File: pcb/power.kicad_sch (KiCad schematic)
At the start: 30 parts, among them U3 TLV75533PDBVR, U4 BQ24078RGTR

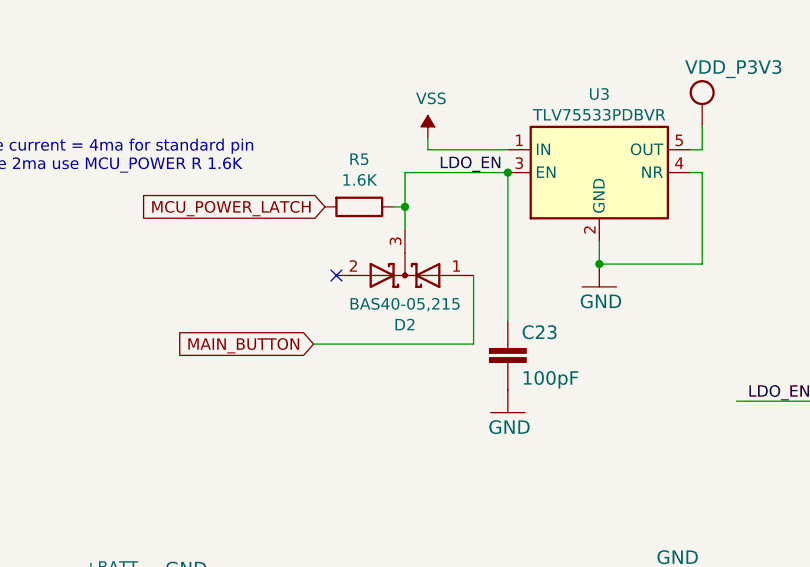
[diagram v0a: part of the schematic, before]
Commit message: [pcb] fixed symbol table issue
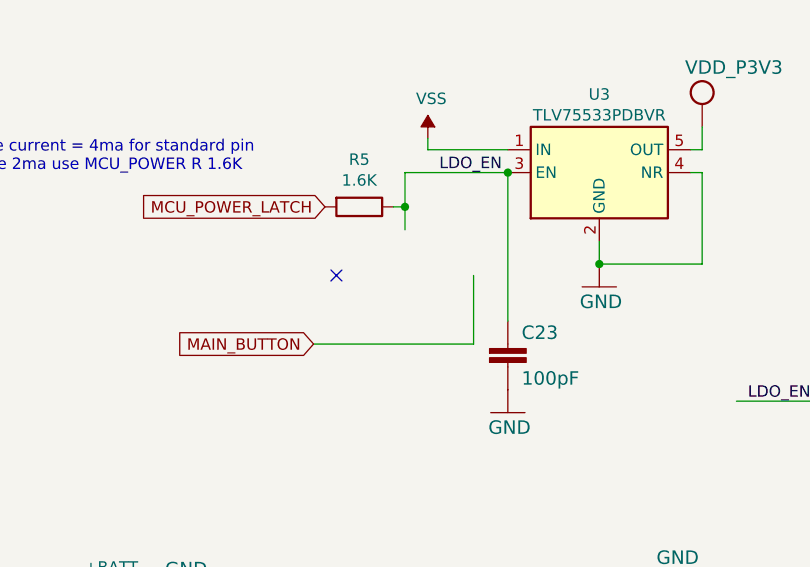
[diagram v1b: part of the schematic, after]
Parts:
- removed D2: BAS40-05,215, Package_TO_SOT_SMD:SOT-23, symbol nRF52832_qfaa-rescue:D_Schottky_x2_KCom_AAK-Device
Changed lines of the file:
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@@
     (pin "1")
-  )
-  (symbol (lib_id "nRF52832_qfaa-rescue:D_Schottky_x2_KCom_AAK-Device") (at 160.02 35.56 180) (unit 1)
-    (in_bom yes) (on_board yes)
-    (property "Reference" "D2" (id 0) (at 160.02 41.0718 0))
-    (property "Value" "BAS40-05,215" (id 1) (at 160.02 38.7604 0))
-    (property "Footprint" "Package_TO_SOT_SMD:SOT-23" (id 2) (at 160.02 35.56 0)
-      (effects (font (size 1.27 1.27)) hide)
-    )
-    (property "Datasheet" "~" (id 3) (at 160.02 35.56 0)
-      (effects (font (size 1.27 1.27)) hide)
-    )
-    (property "LCSC" "C85391" (id 4) (at 160.02 35.56 0)
-      (effects (font (size 1.27 1.27)) hide)
-    )
-    (pin "1")
-    (pin "2")
-    (pin "3")
   )
   (symbol (lib_id "nRF52832_qfaa-eagle-import:VCC") (at 212.09 16.51 0) (unit 1)

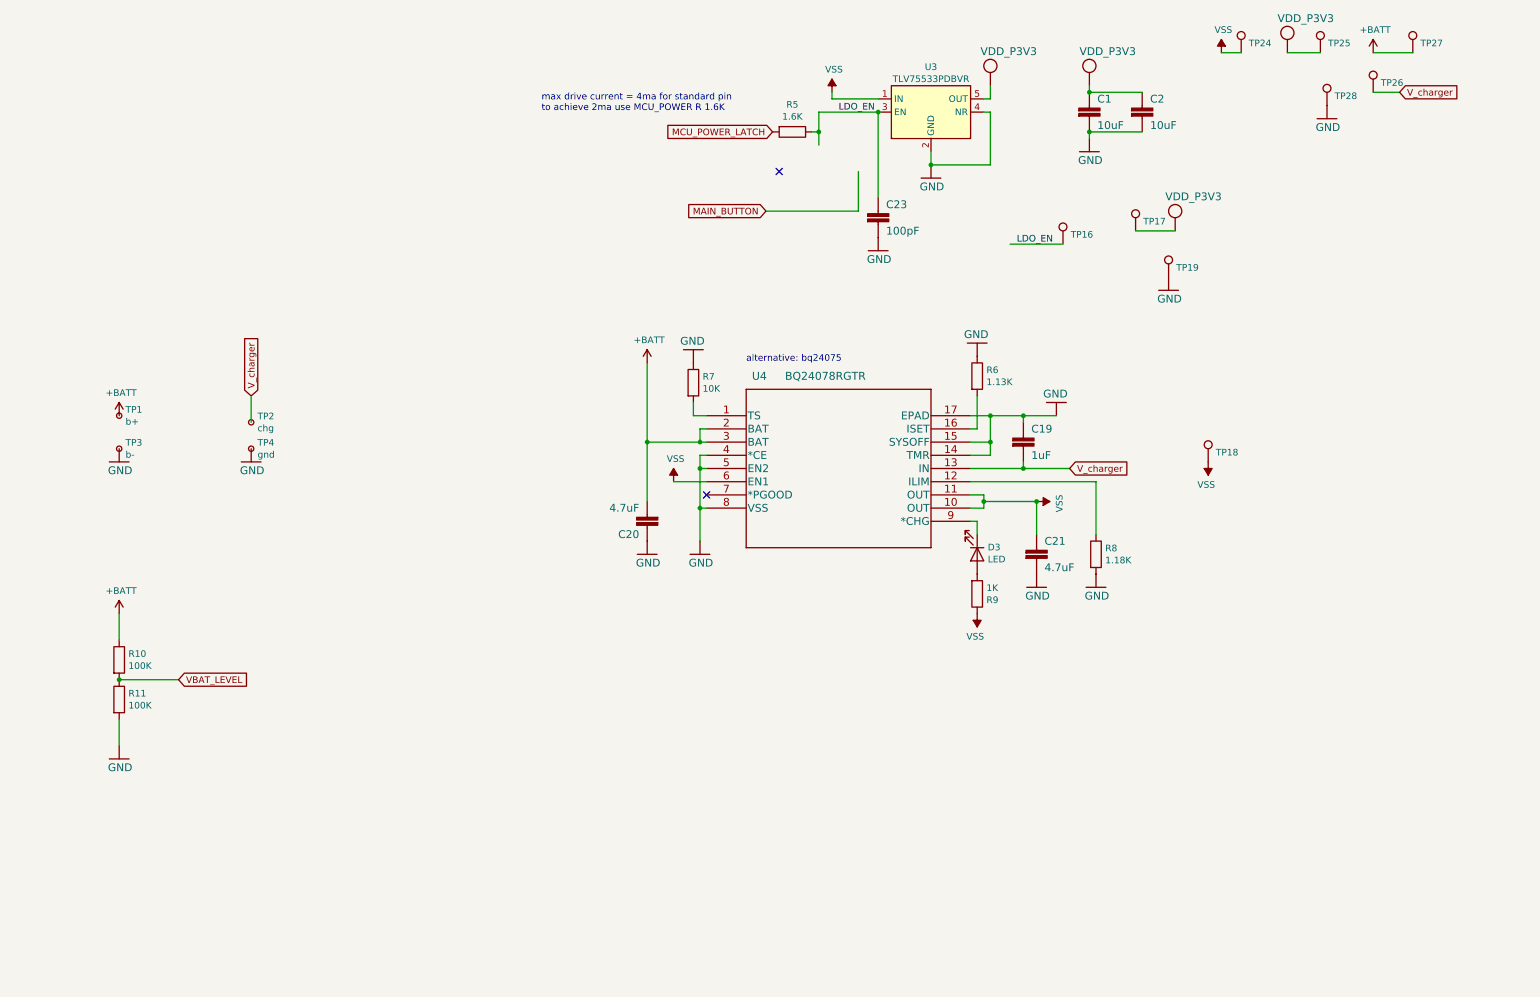
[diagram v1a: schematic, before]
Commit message: [pcb] finalizing layout of v1.3, only testpoints, teardrops and DRC is left
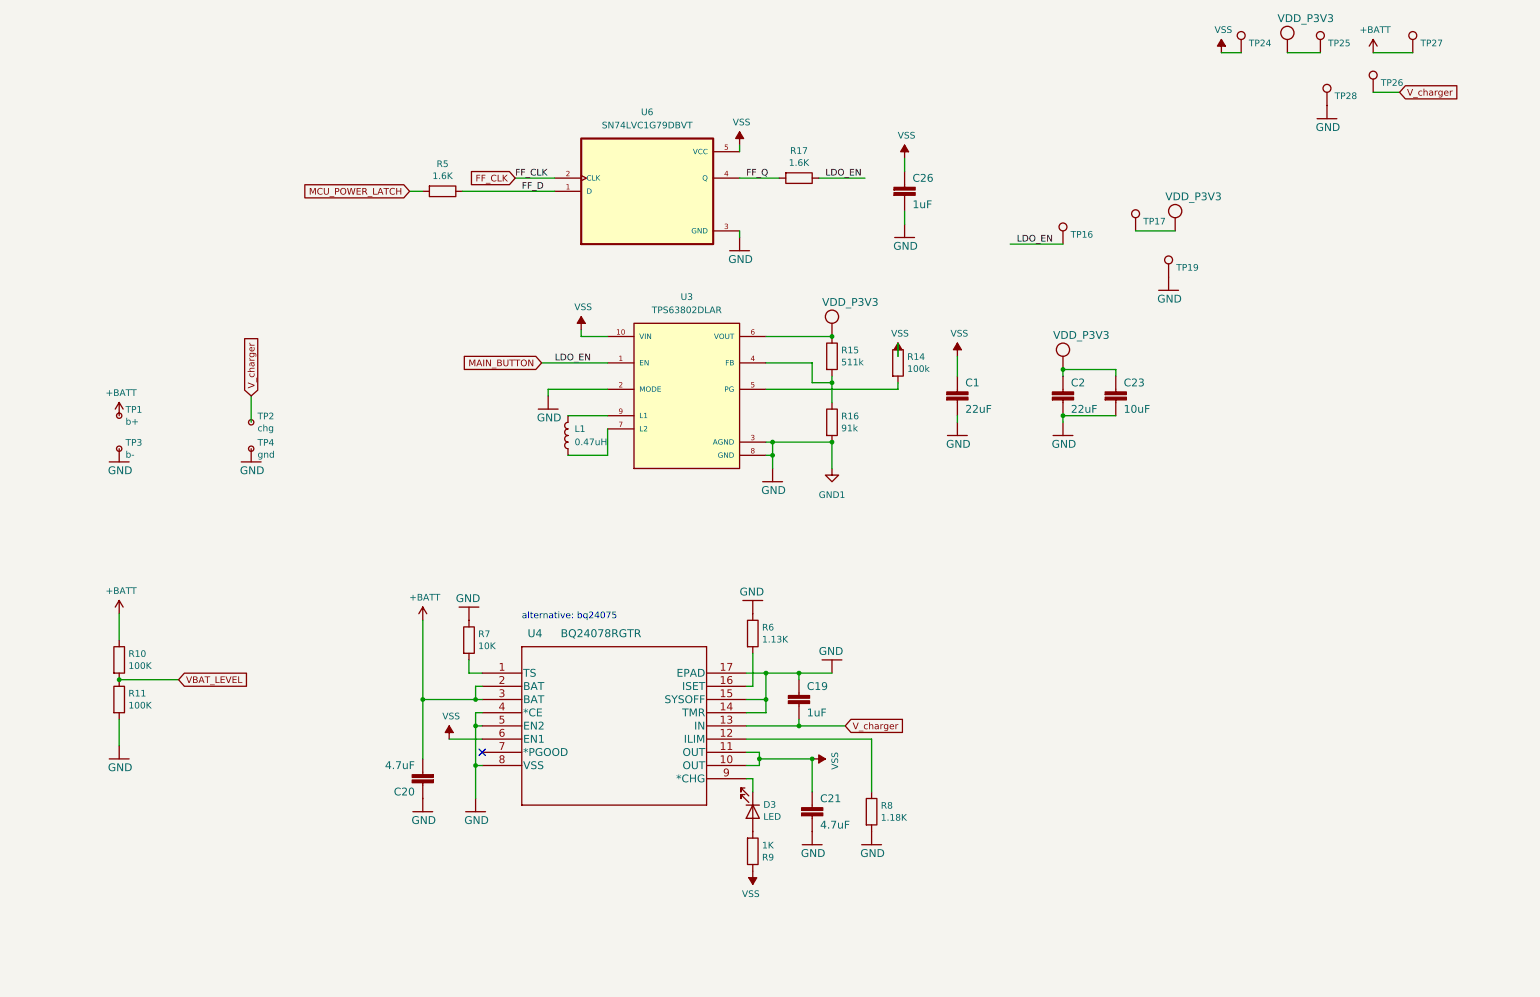
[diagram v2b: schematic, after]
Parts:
- removed TP18: TestPoint, TestPoint:TestPoint_Pad_D1.0mm, symbol Connector:TestPoint
- removed U3: TLV75533PDBVR, Package_TO_SOT_SMD:SOT-23-5, symbol Regulator_Linear:TPS73133DBV
- added C26: 1uF, Capacitor_SMD:C_0402_1005Metric, symbol nRF52832_qfaa-eagle-import:CAPACITOR_0402_N
- added L1: 0.47uH, Inductor_SMD:L_1008_2520Metric, symbol Device:L
- added R14: 100k, Resistor_SMD:R_0402_1005Metric, symbol Device:R
- added R15: 511k, Resistor_SMD:R_0402_1005Metric, symbol Device:R
- added R16: 91k, Resistor_SMD:R_0402_1005Metric, symbol Device:R
- added R17: 1.6K, Resistor_SMD:R_0402_1005Metric, symbol Device:R
- added U3: TPS63802DLAR, VREG_TPS63802DLAR, symbol custom:TPS63802DLAR
- added U6: SN74LVC1G79DBVT, Package_TO_SOT_SMD:SOT-23-5, symbol custom:SN74LVC1G79DBVT
- C1, C2: value 10uF -> 22uF; footprint Capacitor_SMD:C_0402_1005Metric -> Capacitor_SMD:C_0603_1608Metric; LCSC C15525 -> (none)
- C23: value 100pF -> 10uF; LCSC C1546 -> C15525
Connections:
- net GND: now also C26.2, R16.2, U3.2 (MODE), U3.3 (AGND), U3.8 (GND), U6.3 (GND)
- net MAIN_BUTTON: now also TP16.1, R17.1, U3.1 (EN)
- net VCC: now also C23.1, R15.1, U3.6 (VOUT); no longer C1.1
- net VSS: now also C1.1, C26.1, R14.1, U3.10 (VIN), U6.5 (VCC)
- removed net LDO_EN: C23.1, R5.1, TP16.1
- new net: R15.2, R16.1, U3.4 (FB)
- new net: R14.2, U3.5 (PG)
- new net: L1.1, U3.7 (L2)
- new net: L1.2, U3.9 (L1)
- new net FF_CLK: U6.2 (CLK)
- new net FF_D: R5.1, U6.1 (D)
- new net FF_Q: R17.2, U6.4 (Q)
- no-connect marks 2 -> 1
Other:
- note removed: "max drive current = 4ma for standard pin to achieve 2ma use MCU_POWER R 1.6K"
- moved on the sheet: C19, C20, C21, D3, R6, R7, R8, R9, U4

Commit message: [pcb] finalized layout of v1.3
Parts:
- removed TP17: TestPoint, TestPoint:TestPoint_Pad_D1.0mm, symbol Connector:TestPoint
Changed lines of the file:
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@@
-    (stroke (width 0) (type default) (color 0 0 0 0))
-  )
-  (wire (pts (xy 220.98 46.99) (xy 228.6 46.99))
     (stroke (width 0) (type default) (color 0 0 0 0))
   )
@@
     (pin "2")
   )
-  (symbol (lib_id "nRF52832_qfaa-eagle-import:VCC") (at 228.6 44.45 0) (unit 1)
-    (in_bom yes) (on_board yes)
-    (property "Reference" "#VDD_NRF01" (id 0) (at 228.6 44.45 0)
-      (effects (font (size 1.27 1.27)) hide)
-    )
-    (property "Value" "VDD_P3V3" (id 1) (at 226.695 41.275 0)
-      (effects (font (size 1.4986 1.4986)) (justify left bottom))
-    )
-    (property "Footprint" "" (id 2) (at 228.6 44.45 0)
-      (effects (font (size 1.27 1.27)) hide)
-    )
-    (property "Datasheet" "" (id 3) (at 228.6 44.45 0)
-      (effects (font (size 1.27 1.27)) hide)
-    )
-    (pin "1")
-  )
   (symbol (lib_id "Connector:TestPoint") (at 274.32 12.7 0) (unit 1)
     (in_bom yes) (on_board yes)
@@
     (pin "5")
   )
-  (symbol (lib_id "Connector:TestPoint") (at 220.98 46.99 0) (unit 1)
-    (in_bom yes) (on_board yes)
-    (property "Reference" "TP17" (id 0) (at 222.4532 45.1612 0)
-      (effects (font (size 1.27 1.27)) (justify left))
-    )
-    (property "Value" "TestPoint" (id 1) (at 222.4532 46.3042 0)
-      (effects (font (size 1.27 1.27)) (justify left) hide)
-    )
-    (property "Footprint" "TestPoint:TestPoint_Pad_D1.0mm" (id 2) (at 226.06 46.99 0)
-      (effects (font (size 1.27 1.27)) hide)
-    )
-    (property "Datasheet" "~" (id 3) (at 226.06 46.99 0)
-      (effects (font (size 1.27 1.27)) hide)
-    )
-    (pin "1")
-  )
   (symbol (lib_id "nRF52832_qfaa-eagle-import:VCC") (at 207.01 71.12 0) (unit 1)

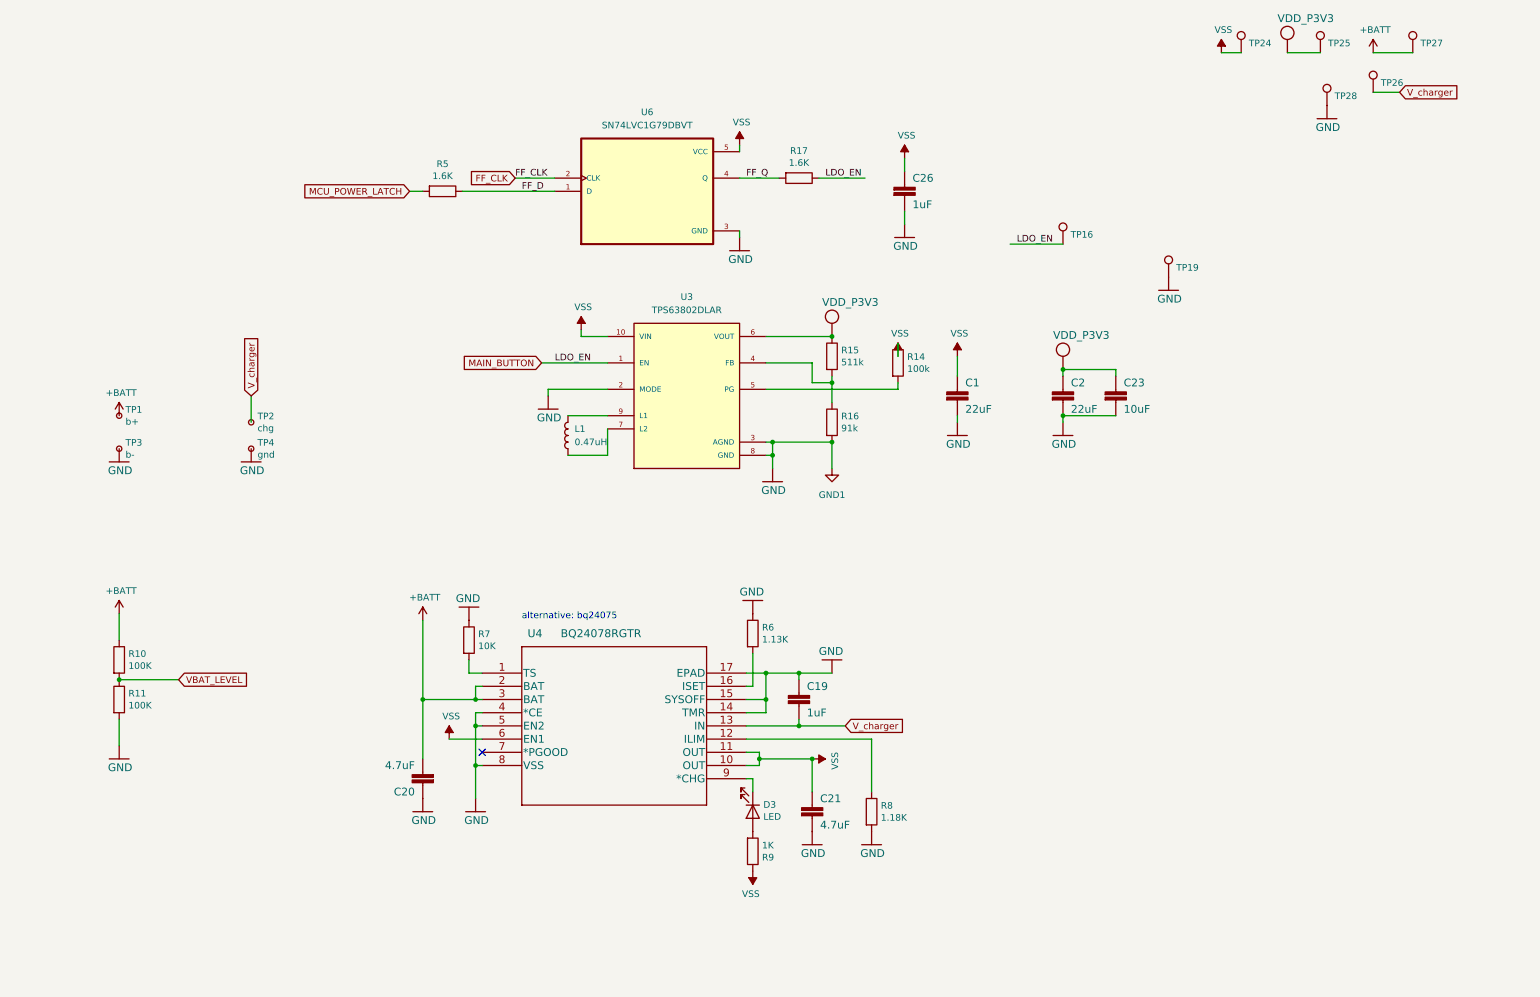
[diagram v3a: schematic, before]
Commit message: [pcb] finalized 1.3: added testpoints, fixed DRC errors
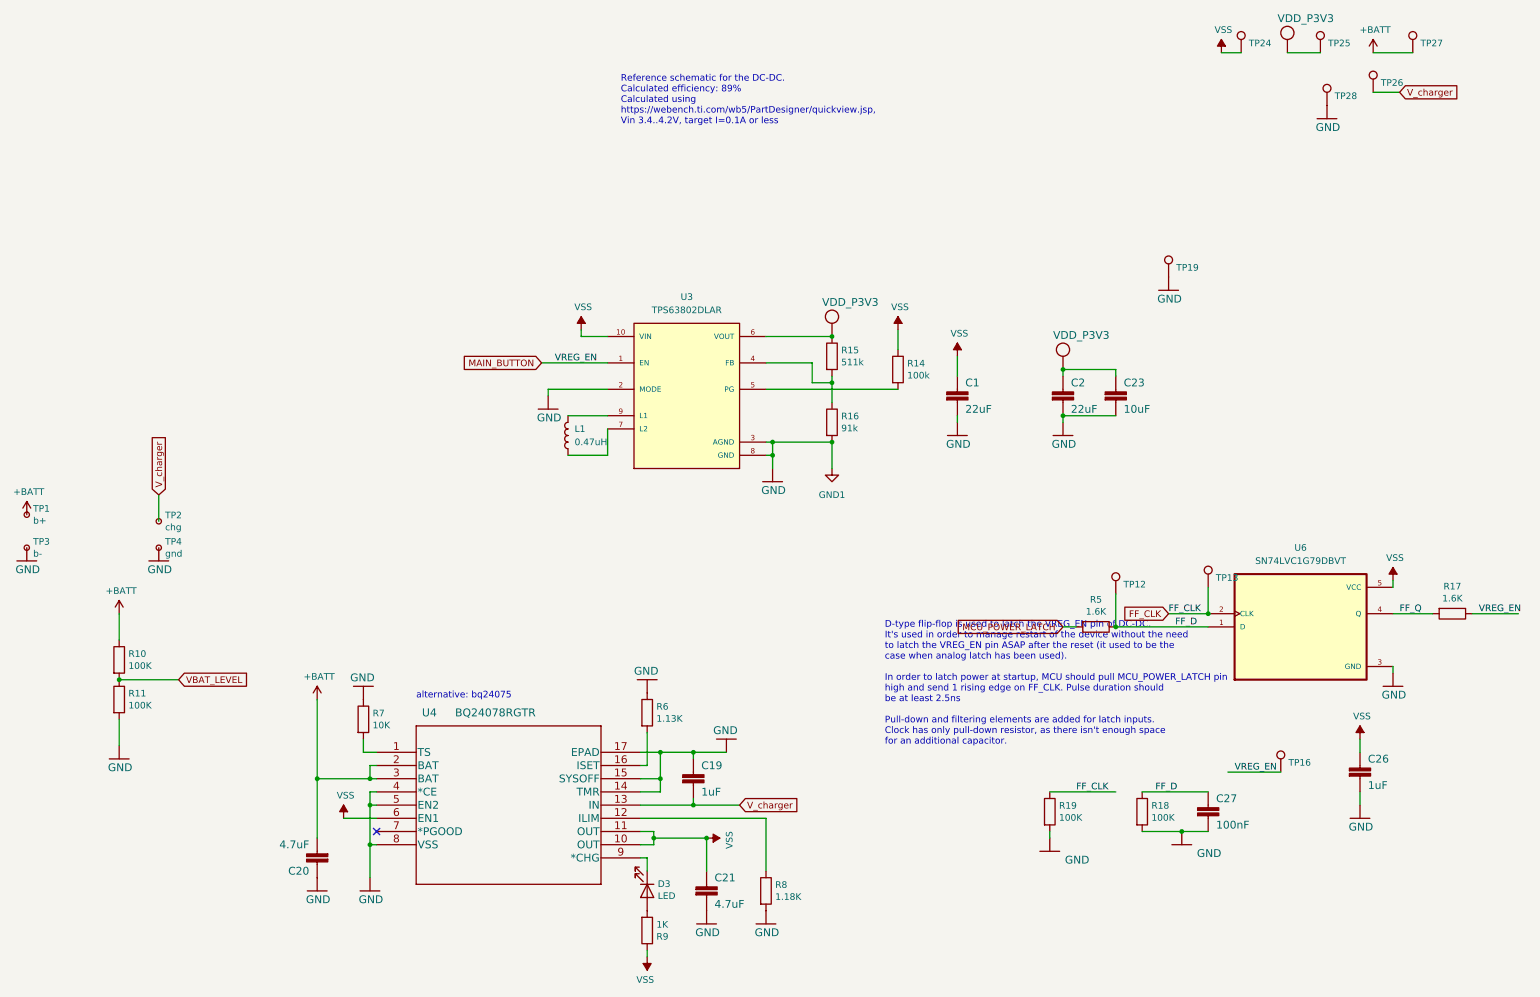
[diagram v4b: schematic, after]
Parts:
- added C27: 100nF, Capacitor_SMD:C_0402_1005Metric, symbol nRF52832_qfaa-eagle-import:CAPACITOR_0402_N
- added R18, R19: 100K, Resistor_SMD:R_0402_1005Metric, symbol Device:R
- added TP12, TP13: TestPoint, TestPoint:TestPoint_Pad_D1.0mm, symbol Connector:TestPoint
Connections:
- net FF_CLK: now also R19.1, TP13.1
- net FF_D: now also C27.1, R18.1, TP12.1
- net GND: now also C27.2, R18.2, R19.2
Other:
- note added: "D-type flip-flop is used to latch the VREG_EN pin of DC-DC. It's used in order to manage restart of the device without the need to latch the VREG_EN pin ASAP after the reset (it used to be the case when analog latch has been used). In order to latch power at startup, MCU should pull MCU_POWER_LATCH pin high and send 1 rising edge on FF_CLK. Pulse duration should be at least 2.5ns Pull-down and fi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"
- note added: "Reference schematic for the DC-DC. Calculated efficiency: 89% Calculated using https://webench.ti.com/wb5/PartDesigner/quickview.jsp, Vin 3.4..4.2V, target I=0.1A or less"
- moved on the sheet: C19, C20, C21, C26, D3, R14, R17, R5, R6, R7, R8, R9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
